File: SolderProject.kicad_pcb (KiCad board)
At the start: 2 copper layers, 60 x 39.5 mm, 19 parts, among them U1 NE555P, U2 4017

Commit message: V1
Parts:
- added G***: LOGO, LOGO, B.Cu at (145.6, 90.2)
- added G***: LOGO, LOGO, B.Cu at (115.2, 83.0)
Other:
- board text added: "Join IEEE!"
- board text added: "Learn about this project on Github"

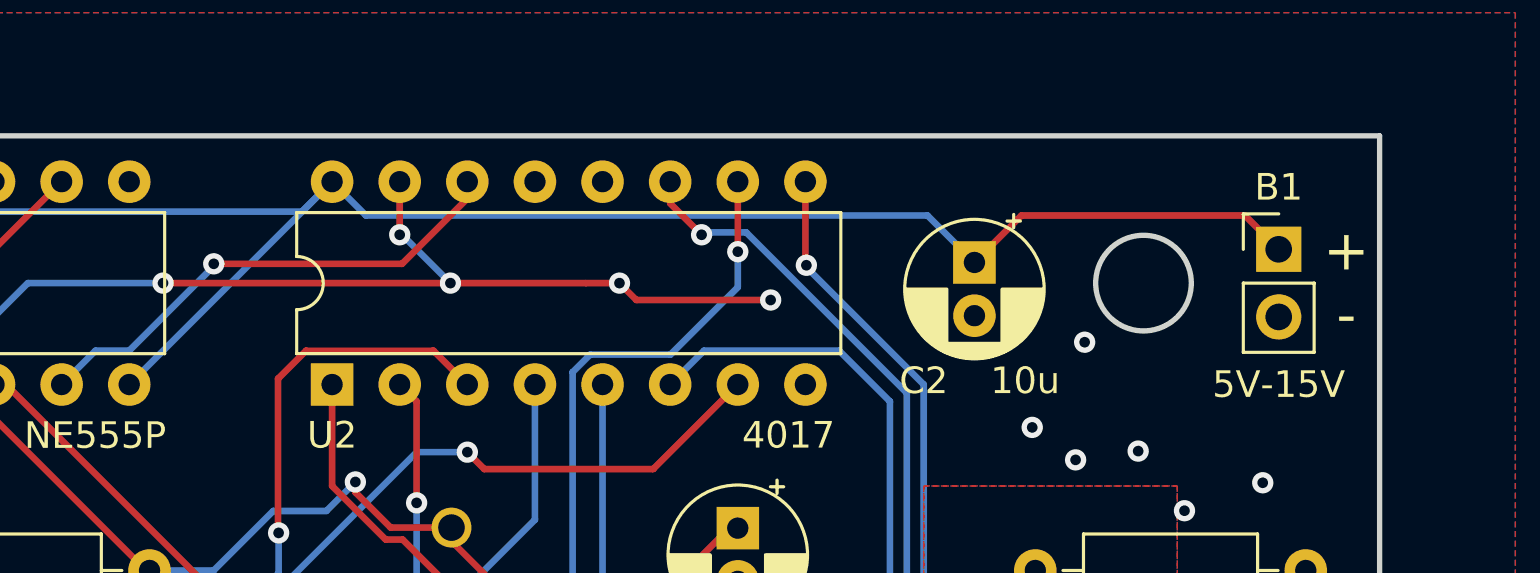
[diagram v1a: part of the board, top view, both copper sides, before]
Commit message: V1.1 - Slight improvements VMax changed to 14V
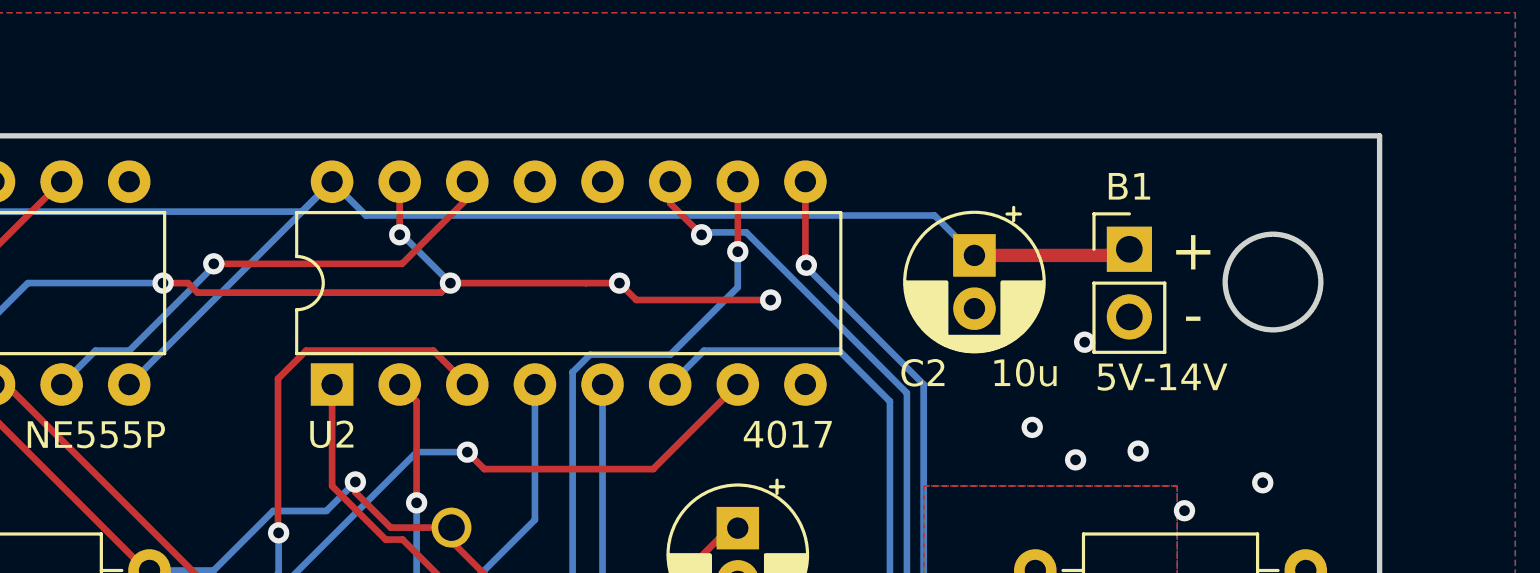
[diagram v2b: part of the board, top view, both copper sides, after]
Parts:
- B1: value 5V-15V -> 5V-14V
- moved B1 5.61 mm to (150.6, 64.8)
- moved C2 0.26 mm to (144.8, 65.0)
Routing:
- net VCC: track 80.4 -> 73.5 mm
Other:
- outline, holes or cut-outs redrawn
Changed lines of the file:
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@@
   )
   (footprint "Connector_PinHeader_2.54mm:PinHeader_1x02_P2.54mm_Vertical" (layer "F.Cu")
-    (at 156.21 64.77)
+    (at 150.6 64.77)
     (descr "Through hole straight pin header, 1x02, 2.54mm pitch, single row")
     (tags "Through hole pin header THT 1x02 2.54mm single row")
@@
       (effects (font (size 1 1) (thickness 0.15)))
     )
-    (fp_text value "5V-15V" (at 0 5.08) (layer "F.SilkS")
+    (fp_text value "5V-14V" (at 1.2 4.83) (layer "F.SilkS")
       (effects (font (size 1 1) (thickness 0.15)))
     )
@@
   )
   (footprint "Capacitor_THT:CP_Radial_D5.0mm_P2.00mm" (layer "F.Cu")
-    (at 144.78 65.26444 -90)
+    (at 144.78 65 -90)
     (descr "CP, Radial series, Radial, pin pitch=2.00mm, , diameter=5mm, Electrolytic Capacitor")
     (tags "CP Radial series Radial pin pitch 2.00mm  diameter 5mm Electrolytic Capacitor")
@@
   )
   (gr_rect (start 100 60.508) (end 160 100) (layer "Edge.Cuts") (width 0.2) (fill none))
-  (gr_circle (center 151.13 66.04) (end 152.926051 66.04) (layer "Edge.Cuts") (width 0.2) (fill none))
+  (gr_circle (center 155.996051 66) (end 157.792102 66) (layer "Edge.Cuts") (width 0.2) (fill none))
   (gr_text "Join IEEE!" (at 125.6 81.6) (layer "B.SilkS")
     (effects (font (size 1.5 1.5) (thickness 0.3)) (justify mirror))
@@
     (effects (font (size 1.2 1.2) (thickness 0.2)) (justify mirror))
   )
-  (gr_text "+\n-" (at 158.75 66.04) (layer "B.SilkS")
+  (gr_text "+\n-" (at 153 66.04) (layer "B.SilkS")
     (effects (font (size 1.5 1.5) (thickness 0.3)) (justify mirror))
   )
-  (gr_text "+\n-" (at 158.75 66.04) (layer "F.SilkS")
+  (gr_text "+\n-" (at 153 66.04) (layer "F.SilkS")
     (effects (font (size 1.5 1.5) (thickness 0.3)))
   )
@@
   (segment (start 124.324 77.724) (end 125.975 79.375) (width 0.25) (layer "F.Cu") (net 1))
   (segment (start 122.381 77.47) (end 116.017991 77.47) (width 0.25) (layer "F.Cu") (net 1))
+  (segment (start 124.735 66.4) (end 125.095 66.04) (width 0.25) (layer "F.Cu") (net 2))
+  (segment (start 114.3 66.04) (end 115.24 66.04) (width 0.25) (layer "F.Cu") (net 2))
   (segment (start 132.08 66.675) (end 137.123951 66.675) (width 0.25) (layer "F.Cu") (net 2))
   (segment (start 130.175 66.04) (end 131.445 66.04) (width 0.25) (layer "F.Cu") (net 2))
   (segment (start 131.445 66.04) (end 132.08 66.675) (width 0.25) (layer "F.Cu") (net 2))
-  (segment (start 114.3 66.04) (end 125.095 66.04) (width 0.25) (layer "F.Cu") (net 2))
+  (segment (start 115.6 66.4) (end 124.735 66.4) (width 0.25) (layer "F.Cu") (net 2))
   (segment (start 125.095 66.04) (end 130.175 66.04) (width 0.25) (layer "F.Cu") (net 2))
   (segment (start 123.19 64.2245) (end 123.19 62.23) (width 0.25) (layer "F.Cu") (net 2))
+  (segment (start 115.24 66.04) (end 115.6 66.4) (width 0.25) (layer "F.Cu") (net 2))
   (via (at 148.92 68.26) (size 0.8) (drill 0.4) (layers "F.Cu" "B.Cu") (free) (net 2))
   (via (at 131.445 66.04) (size 0.8) (drill 0.4) (layers "F.Cu" "B.Cu") (net 2))
@@
   (segment (start 116.205 65.3155) (end 116.205 65.405) (width 0.25) (layer "B.Cu") (net 3))
   (segment (start 111.76 68.58) (end 110.49 69.85) (width 0.25) (layer "B.Cu") (net 3))
-  (segment (start 144.78 65.26444) (end 146.54444 63.5) (width 0.25) (layer "F.Cu") (net 4))
-  (segment (start 146.54444 63.5) (end 154.94 63.5) (width 0.25) (layer "F.Cu") (net 4))
-  (segment (start 154.94 63.5) (end 156.21 64.77) (width 0.25) (layer "F.Cu") (net 4))
+  (segment (start 144.78 65) (end 150.37 65) (width 0.5) (layer "F.Cu") (net 4))
+  (segment (start 150.37 65) (end 150.6 64.77) (width 0.25) (layer "F.Cu") (net 4))
   (segment (start 113.03 69.85) (end 120.65 62.23) (width 0.25) (layer "B.Cu") (net 4))
-  (segment (start 143.01556 63.5) (end 121.92 63.5) (width 0.25) (layer "B.Cu") (net 4))
   (segment (start 105.41 62.23) (end 106.535 63.355) (width 0.25) (layer "B.Cu") (net 4))
-  (segment (start 144.78 65.26444) (end 143.01556 63.5) (width 0.25) (layer "B.Cu") (net 4))
-  (segment (start 121.92 63.5) (end 120.65 62.23) (width 0.25) (layer "B.Cu") (net 4))
+  (segment (start 143.28 63.5) (end 121.92 63.5) (width 0.25) (layer "B.Cu") (net 4))
+  (segment (start 144.78 65) (end 143.28 63.5) (width 0.25) (layer "B.Cu") (net 4))
   (segment (start 105.41 62.23) (end 103.632 64.008) (width 0.25) (layer "B.Cu") (net 4))
   (segment (start 119.525 63.355) (end 120.65 62.23) (width 0.25) (layer "B.Cu") (net 4))
+  (segment (start 121.92 63.5) (end 120.65 62.23) (width 0.25) (layer "B.Cu") (net 4))
   (segment (start 106.535 63.355) (end 119.525 63.355) (width 0.25) (layer "B.Cu") (net 4))
   (segment (start 103.632 64.008) (end 103.632 76.835) (width 0.25) (layer "B.Cu") (net 4))
